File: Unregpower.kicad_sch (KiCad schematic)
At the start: 22 parts, among them J10 Conn_01x03_Female, J11 Conn_01x08_Female, J12 Conn_01x03_Female, J13 Conn_01x08_Female, J14 Conn_01x03_Female

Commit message: last TH mounting board
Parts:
- C21, C22, C26: renamed from C?; footprint (none) -> Capacitor_SMD:C_0603_1608Metric
- C23: renamed from C1; footprint Capacitor_THT:CP_Radial_D8.0mm_P3.50mm -> Capacitor_SMD:C_Elec_8x6.2; Availability (none) -> Back order
- C24: renamed from C2; footprint Capacitor_THT:CP_Radial_D8.0mm_P3.50mm -> Capacitor_SMD:C_Elec_8x6.2; Availability (none) -> Back order
- C25: renamed from C?; value C_Small -> 0.1uF; footprint (none) -> Capacitor_SMD:C_0603_1608Metric
- D1, D2, D3, D4, D5, D6: value D -> S1K-13-F; footprint Diode_THT:D_T-1_P10.16mm_Horizontal -> Diode_SMD:D_SMA
- TR1: Availability (none) -> Arrived
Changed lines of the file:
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@@
       (effects (font (size 1.27 1.27)) (justify left))
     )
-    (property "Value" "D" (id 1) (at 114.808 93.853 90)
-      (effects (font (size 1.27 1.27)) (justify left))
-    )
-    (property "Footprint" "Diode_THT:D_T-1_P10.16mm_Horizontal" (id 2) (at 112.776 94.996 0)
+    (property "Value" "S1K-13-F" (id 1) (at 114.808 93.853 90)
+      (effects (font (size 1.27 1.27)) (justify left))
+    )
+    (property "Footprint" "Diode_SMD:D_SMA" (id 2) (at 112.776 94.996 0)
       (effects (font (size 1.27 1.27)) hide)
     )
@@
       (effects (font (size 1.27 1.27)) (justify right))
     )
-    (property "Value" "D" (id 1) (at 126.238 93.853 90)
-      (effects (font (size 1.27 1.27)) (justify right))
-    )
-    (property "Footprint" "Diode_THT:D_T-1_P10.16mm_Horizontal" (id 2) (at 124.206 94.996 0)
+    (property "Value" "S1K-13-F" (id 1) (at 126.238 93.853 90)
+      (effects (font (size 1.27 1.27)) (justify right))
+    )
+    (property "Footprint" "Diode_SMD:D_SMA" (id 2) (at 124.206 94.996 0)
       (effects (font (size 1.27 1.27)) hide)
     )
@@
   (symbol (lib_id "power:PWR_FLAG") (at 102.616 107.696 90) (unit 1)
     (in_bom yes) (on_board yes)
-    (property "Reference" "#FLG05" (id 0) (at 100.711 107.696 0)
+    (property "Reference" "#FLG04" (id 0) (at 100.711 107.696 0)
       (effects (font (size 1.27 1.27)) hide)
     )
@@
       (effects (font (size 1.27 1.27)) (justify right))
     )
-    (property "Value" "D" (id 1) (at 110.744 86.233 90)
-      (effects (font (size 1.27 1.27)) (justify right))
-    )
-    (property "Footprint" "Diode_THT:D_T-1_P10.16mm_Horizontal" (id 2) (at 112.776 87.376 0)
+    (property "Value" "S1K-13-F" (id 1) (at 110.744 86.233 90)
+      (effects (font (size 1.27 1.27)) (justify right))
+    )
+    (property "Footprint" "Diode_SMD:D_SMA" (id 2) (at 112.776 87.376 0)
       (effects (font (size 1.27 1.27)) hide)
     )
@@
   (symbol (lib_id "minipowersupply-rescue:CP-Device") (at 121.666 114.046 0) (unit 1)
     (in_bom yes) (on_board yes)
-    (property "Reference" "C2" (id 0) (at 124.6632 112.8776 0)
+    (property "Reference" "C24" (id 0) (at 124.6632 112.8776 0)
       (effects (font (size 1.27 1.27)) (justify left))
     )
@@
       (effects (font (size 1.27 1.27)) (justify left))
     )
-    (property "Footprint" "Capacitor_THT:CP_Radial_D8.0mm_P3.50mm" (id 2) (at 122.6312 117.856 0)
+    (property "Footprint" "Capacitor_SMD:C_Elec_8x6.2" (id 2) (at 122.6312 117.856 0)
       (effects (font (size 1.27 1.27)) hide)
     )
@@
       (effects (font (size 1.27 1.27)) hide)
     )
+    (property "Availability" "Back order" (id 4) (at 121.666 114.046 0)
+      (effects (font (size 1.27 1.27)) hide)
+    )
     (pin "1")
     (pin "2")
@@
       (effects (font (size 1.27 1.27)) (justify left))
     )
-    (property "Value" "D" (id 1) (at 126.238 86.233 90)
-      (effects (font (size 1.27 1.27)) (justify left))
-    )
-    (property "Footprint" "Diode_THT:D_T-1_P10.16mm_Horizontal" (id 2) (at 124.206 87.376 0)
+    (property "Value" "S1K-13-F" (id 1) (at 126.238 86.233 90)
+      (effects (font (size 1.27 1.27)) (justify left))
+    )
+    (property "Footprint" "Diode_SMD:D_SMA" (id 2) (at 124.206 87.376 0)
       (effects (font (size 1.27 1.27)) hide)
     )
@@
   (symbol (lib_id "Device:C_Small") (at 187.452 83.566 0) (unit 1)
     (in_bom yes) (on_board yes) (fields_autoplaced)
-    (property "Reference" "C?" (id 0) (at 189.7761 82.7376 0)
+    (property "Reference" "C21" (id 0) (at 189.7761 82.7376 0)
       (effects (font (size 1.27 1.27)) (justify left))
     )
@@
       (effects (font (size 1.27 1.27)) (justify left))
     )
-    (property "Footprint" "" (id 2) (at 187.452 83.566 0)
+    (property "Footprint" "Capacitor_SMD:C_0603_1608Metric" (id 2) (at 187.452 83.566 0)
       (effects (font (size 1.27 1.27)) hide)
     )
@@
     (in_bom yes) (on_board yes)
     (property "Reference" "D1" (id 0) (at 135.636 78.0542 0))
-    (property "Value" "D" (id 1) (at 135.636 80.3656 0))
-    (property "Footprint" "Diode_THT:D_T-1_P10.16mm_Horizontal" (id 2) (at 135.636 83.566 0)
+    (property "Value" "S1K-13-F" (id 1) (at 135.636 80.3656 0))
+    (property "Footprint" "Diode_SMD:D_SMA" (id 2) (at 135.636 83.566 0)
       (effects (font (size 1.27 1.27)) hide)
     )
@@
   (symbol (lib_id "Device:C_Small") (at 180.594 108.966 0) (unit 1)
     (in_bom yes) (on_board yes) (fields_autoplaced)
-    (property "Reference" "C?" (id 0) (at 182.9181 108.1376 0)
+    (property "Reference" "C22" (id 0) (at 182.9181 108.1376 0)
       (effects (font (size 1.27 1.27)) (justify left))
     )
@@
       (effects (font (size 1.27 1.27)) (justify left))
     )
-    (property "Footprint" "" (id 2) (at 180.594 108.966 0)
+    (property "Footprint" "Capacitor_SMD:C_0603_1608Metric" (id 2) (at 180.594 108.966 0)
       (effects (font (size 1.27 1.27)) hide)
     )
@@
     (in_bom yes) (on_board yes)
     (property "Reference" "D6" (id 0) (at 135.636 101.346 0))
-    (property "Value" "D" (id 1) (at 135.636 96.266 0))
-    (property "Footprint" "Diode_THT:D_T-1_P10.16mm_Horizontal" (id 2) (at 135.636 98.806 0)
+    (property "Value" "S1K-13-F" (id 1) (at 135.636 96.266 0))
+    (property "Footprint" "Diode_SMD:D_SMA" (id 2) (at 135.636 98.806 0)
       (effects (font (size 1.27 1.27)) hide)
     )
@@
   (symbol (lib_id "minipowersupply-rescue:CP-Device") (at 102.616 114.046 180) (unit 1)
     (in_bom yes) (on_board yes)
-    (property "Reference" "C1" (id 0) (at 105.6132 112.8776 0)
+    (property "Reference" "C23" (id 0) (at 105.6132 112.8776 0)
       (effects (font (size 1.27 1.27)) (justify right))
     )
@@
       (effects (font (size 1.27 1.27)) (justify right))
     )
-    (property "Footprint" "Capacitor_THT:CP_Radial_D8.0mm_P3.50mm" (id 2) (at 101.6508 110.236 0)
+    (property "Footprint" "Capacitor_SMD:C_Elec_8x6.2" (id 2) (at 101.6508 110.236 0)
       (effects (font (size 1.27 1.27)) hide)
     )
     (property "Datasheet" "~" (id 3) (at 102.616 114.046 0)
+      (effects (font (size 1.27 1.27)) hide)
+    )
+    (property "Availability" "Back order" (id 4) (at 102.616 114.046 0)
       (effects (font (size 1.27 1.27)) hide)
     )
@@
   (symbol (lib_id "Device:C_Small") (at 185.928 129.286 0) (unit 1)
     (in_bom yes) (on_board yes) (fields_autoplaced)
-    (property "Reference" "C?" (id 0) (at 188.2521 128.4576 0)
+    (property "Reference" "C26" (id 0) (at 188.2521 128.4576 0)
       (effects (font (size 1.27 1.27)) (justify left))
     )
@@
       (effects (font (size 1.27 1.27)) (justify left))
     )
-    (property "Footprint" "" (id 2) (at 185.928 129.286 0)
+    (property "Footprint" "Capacitor_SMD:C_0603_1608Metric" (id 2) (at 185.928 129.286 0)
       (effects (font (size 1.27 1.27)) hide)
     )
@@
   (symbol (lib_id "power:PWR_FLAG") (at 96.266 83.566 0) (unit 1)
     (in_bom yes) (on_board yes)
-    (property "Reference" "#FLG02" (id 0) (at 96.266 81.661 0)
+    (property "Reference" "#FLG01" (id 0) (at 96.266 81.661 0)
       (effects (font (size 1.27 1.27)) hide)
     )
@@
   (symbol (lib_id "Device:C_Small") (at 185.928 119.126 0) (unit 1)
     (in_bom yes) (on_board yes) (fields_autoplaced)
-    (property "Reference" "C?" (id 0) (at 188.2521 118.2976 0)
-      (effects (font (size 1.27 1.27)) (justify left))
-    )
-    (property "Value" "C_Small" (id 1) (at 188.2521 120.8345 0)
-      (effects (font (size 1.27 1.27)) (justify left))
-    )
-    (property "Footprint" "" (id 2) (at 185.928 119.126 0)
+    (property "Reference" "C25" (id 0) (at 188.2521 118.2976 0)
+      (effects (font (size 1.27 1.27)) (justify left))
+    )
+    (property "Value" "0.1uF" (id 1) (at 188.2521 120.8345 0)
+      (effects (font (size 1.27 1.27)) (justify left))
+    )
+    (property "Footprint" "Capacitor_SMD:C_0603_1608Metric" (id 2) (at 185.928 119.126 0)
       (effects (font (size 1.27 1.27)) hide)
     )
@@
   (symbol (lib_id "power:PWR_FLAG") (at 96.266 98.806 0) (unit 1)
     (in_bom yes) (on_board yes)
-    (property "Reference" "#FLG04" (id 0) (at 96.266 96.901 0)
+    (property "Reference" "#FLG03" (id 0) (at 96.266 96.901 0)
       (effects (font (size 1.27 1.27)) hide)
     )
@@
   (symbol (lib_id "power:PWR_FLAG") (at 121.666 107.696 90) (unit 1)
     (in_bom yes) (on_board yes)
-    (property "Reference" "#FLG06" (id 0) (at 119.761 107.696 0)
+    (property "Reference" "#FLG05" (id 0) (at 119.761 107.696 0)
       (effects (font (size 1.27 1.27)) hide)
     )
@@
     )
     (property "Datasheet" "" (id 3) (at 88.646 91.186 0)
+      (effects (font (size 1.27 1.27)) hide)
+    )
+    (property "Availability" "Arrived" (id 4) (at 88.646 91.186 0)
       (effects (font (size 1.27 1.27)) hide)
     )
@@
   (symbol (lib_id "power:PWR_FLAG") (at 96.266 91.186 0) (unit 1)
     (in_bom yes) (on_board yes)
-    (property "Reference" "#FLG03" (id 0) (at 96.266 89.281 0)
-      (effects (font (size 1.27 1.27)) hide)
-    )
+    (property "Reference" "#FLG02" (id 0) (at 96.266 89.281 0)
+      (effects (font (size 1.27 1.27)) hide)
+    )

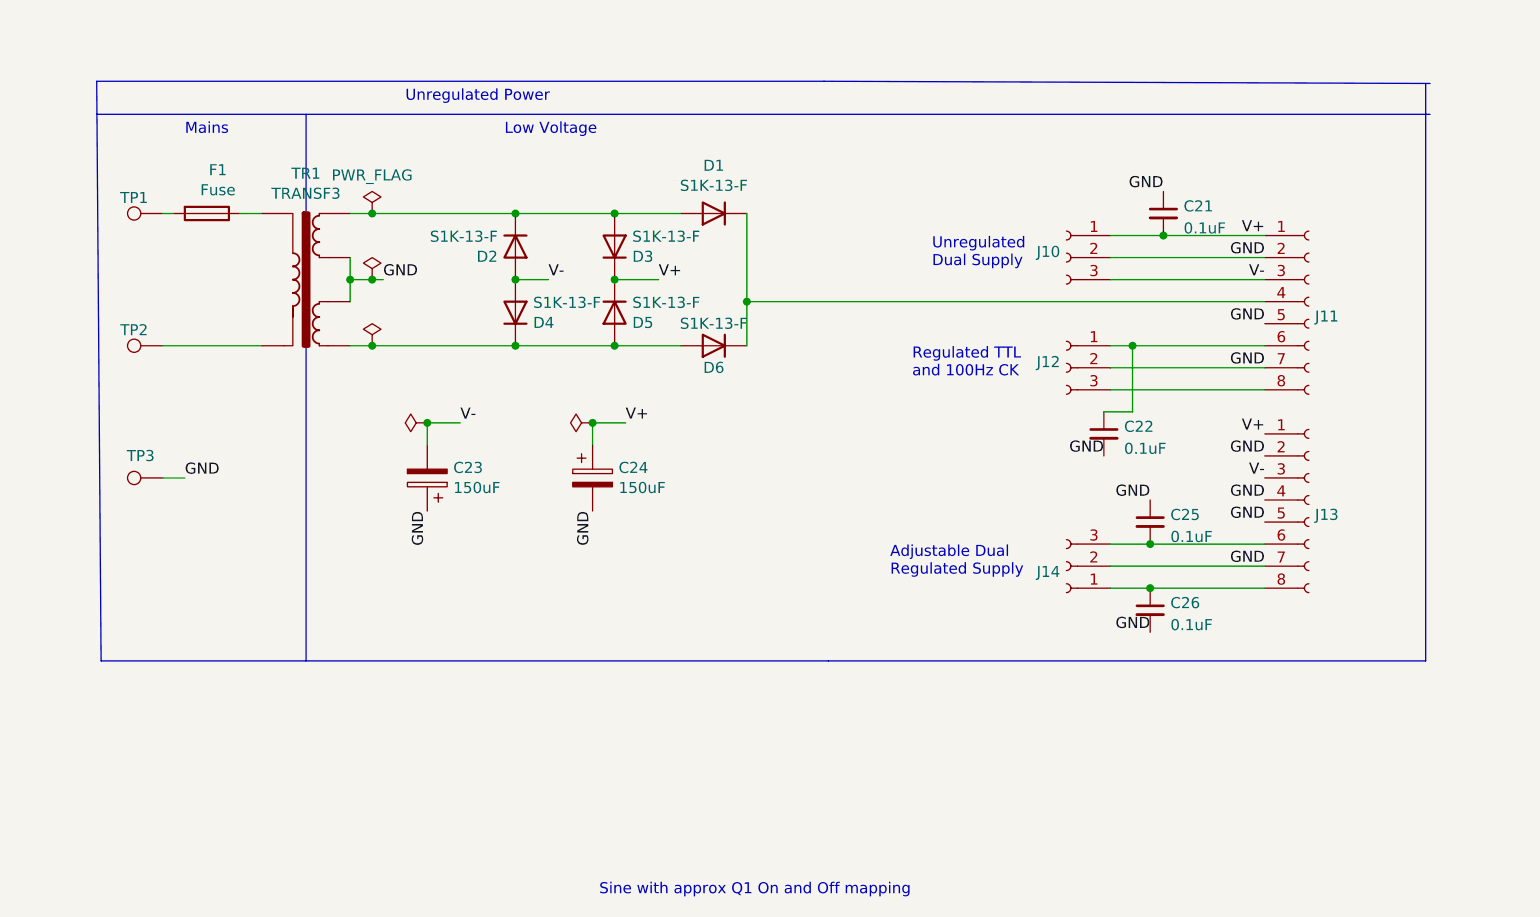
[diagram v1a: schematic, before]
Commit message: all SMD components going into boards
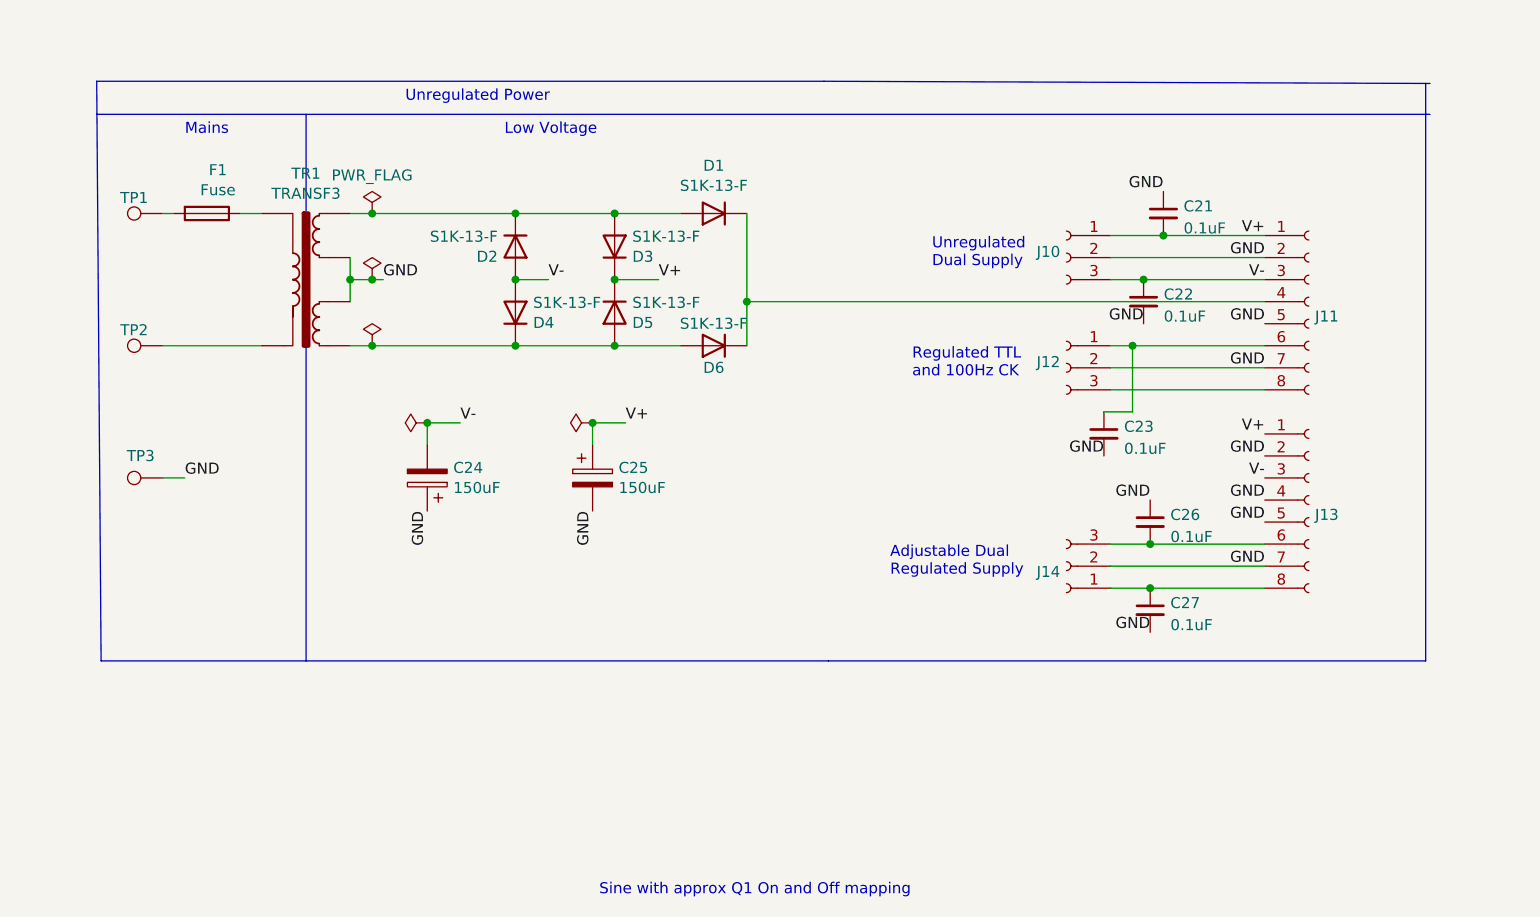
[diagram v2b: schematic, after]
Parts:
- added C22: 0.1uF, Capacitor_SMD:C_0603_1608Metric, symbol Device:C_Small
- renumbered C22 to C23, C23 to C24, C24 to C25, C25 to C26, C26 to C27
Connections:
- net GND: now also C22.2
- net V-: now also C22.1
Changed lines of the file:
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@@
   (junction (at 96.266 98.806) (diameter 0) (color 0 0 0 0)
   )
+  (junction (at 185.166 91.186) (diameter 0) (color 0 0 0 0)
+  )
   (junction (at 124.206 83.566) (diameter 0) (color 0 0 0 0)
   )
@@
     (stroke (width 0) (type default) (color 0 0 0 0))
   )
-  (wire (pts (xy 181.356 91.186) (xy 199.136 91.186))
+  (wire (pts (xy 181.356 91.186) (xy 185.166 91.186))
     (stroke (width 0) (type default) (color 0 0 0 0))
   )
@@
   )
   (wire (pts (xy 112.776 83.566) (xy 124.206 83.566))
+    (stroke (width 0) (type default) (color 0 0 0 0))
+  )
+  (wire (pts (xy 185.166 91.186) (xy 199.136 91.186))
     (stroke (width 0) (type default) (color 0 0 0 0))
   )
@@
     (effects (font (size 1.27 1.27)) (justify right bottom))
   )
+  (label "GND" (at 185.166 96.266 180)
+    (effects (font (size 1.27 1.27)) (justify right bottom))
+  )
   (label "GND" (at 185.928 131.826 180)
     (effects (font (size 1.27 1.27)) (justify right bottom))
@@
     )
     (property "Datasheet" "~" (id 3) (at 112.776 94.996 0)
+      (effects (font (size 1.27 1.27)) hide)
+    )
+    (pin "1")
+    (pin "2")
+  )
+  (symbol (lib_id "Device:C_Small") (at 185.166 93.726 0) (unit 1)
+    (in_bom yes) (on_board yes) (fields_autoplaced)
+    (property "Reference" "C22" (id 0) (at 187.4901 92.8976 0)
+      (effects (font (size 1.27 1.27)) (justify left))
+    )
+    (property "Value" "0.1uF" (id 1) (at 187.4901 95.4345 0)
+      (effects (font (size 1.27 1.27)) (justify left))
+    )
+    (property "Footprint" "Capacitor_SMD:C_0603_1608Metric" (id 2) (at 185.166 93.726 0)
+      (effects (font (size 1.27 1.27)) hide)
+    )
+    (property "Datasheet" "~" (id 3) (at 185.166 93.726 0)
       (effects (font (size 1.27 1.27)) hide)
     )
@@
   (symbol (lib_id "minipowersupply-rescue:CP-Device") (at 121.666 114.046 0) (unit 1)
     (in_bom yes) (on_board yes)
-    (property "Reference" "C24" (id 0) (at 124.6632 112.8776 0)
+    (property "Reference" "C25" (id 0) (at 124.6632 112.8776 0)
       (effects (font (size 1.27 1.27)) (justify left))
     )
@@
   (symbol (lib_id "Device:C_Small") (at 180.594 108.966 0) (unit 1)
     (in_bom yes) (on_board yes) (fields_autoplaced)
-    (property "Reference" "C22" (id 0) (at 182.9181 108.1376 0)
+    (property "Reference" "C23" (id 0) (at 182.9181 108.1376 0)
       (effects (font (size 1.27 1.27)) (justify left))
     )
@@
   (symbol (lib_id "minipowersupply-rescue:CP-Device") (at 102.616 114.046 180) (unit 1)
     (in_bom yes) (on_board yes)
-    (property "Reference" "C23" (id 0) (at 105.6132 112.8776 0)
+    (property "Reference" "C24" (id 0) (at 105.6132 112.8776 0)
       (effects (font (size 1.27 1.27)) (justify right))
     )
@@
   (symbol (lib_id "Device:C_Small") (at 185.928 129.286 0) (unit 1)
     (in_bom yes) (on_board yes) (fields_autoplaced)
-    (property "Reference" "C26" (id 0) (at 188.2521 128.4576 0)
+    (property "Reference" "C27" (id 0) (at 188.2521 128.4576 0)
       (effects (font (size 1.27 1.27)) (justify left))
     )
@@
   (symbol (lib_id "Device:C_Small") (at 185.928 119.126 0) (unit 1)
     (in_bom yes) (on_board yes) (fields_autoplaced)
-    (property "Reference" "C25" (id 0) (at 188.2521 118.2976 0)
-      (effects (font (size 1.27 1.27)) (justify left))
-    )
+    (property "Reference" "C26" (id 0) (at 188.2521 118.2976 0)
+      (effects (font (size 1.27 1.27)) (justify left))
+    )

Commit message: new board with SMD
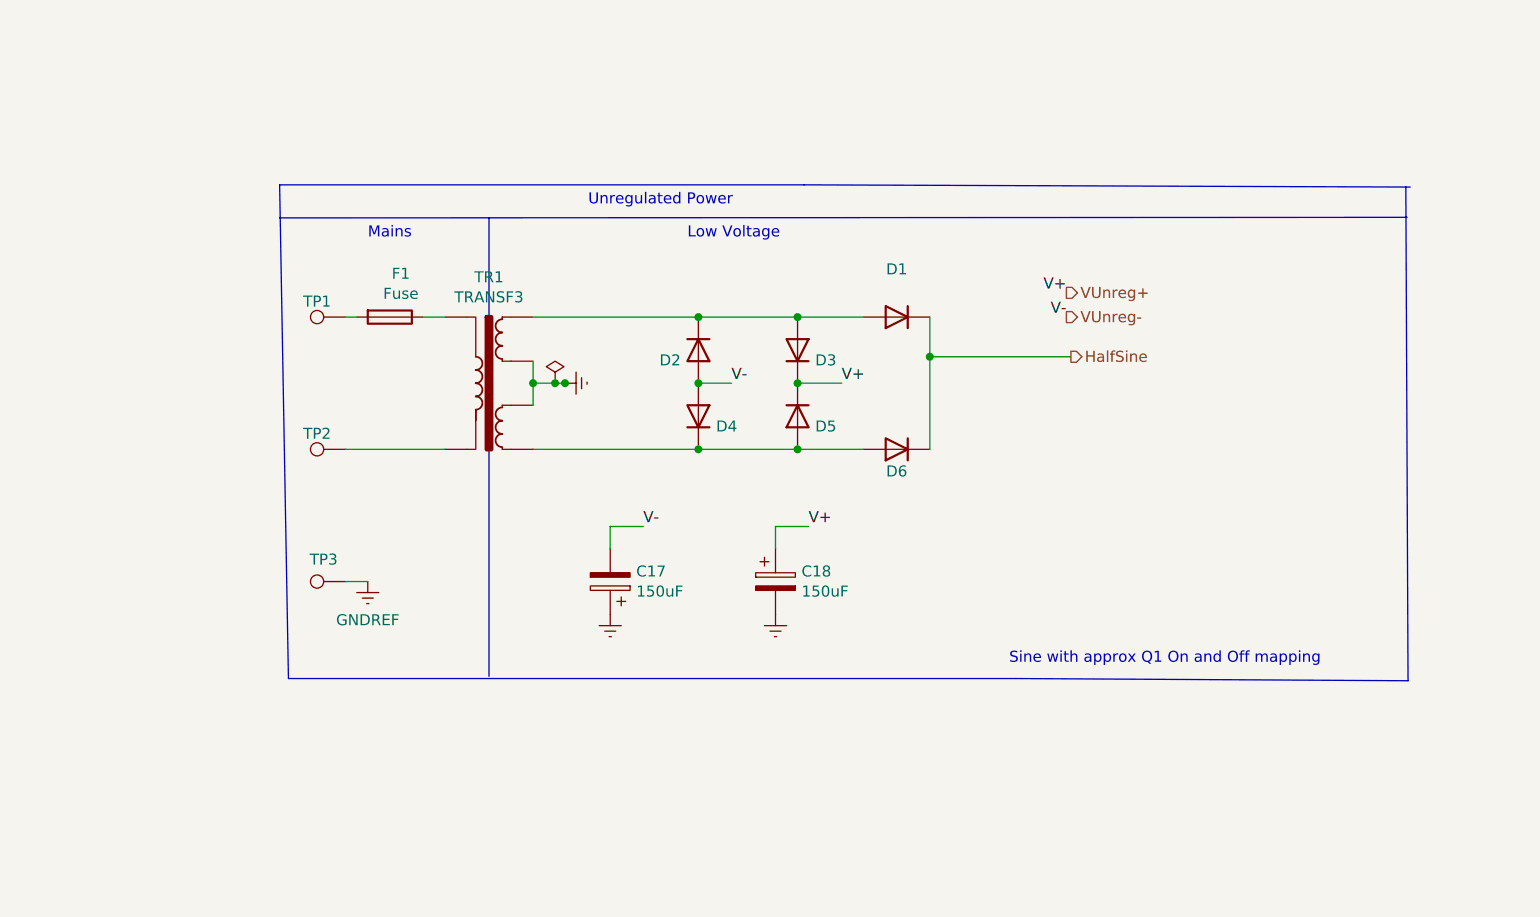
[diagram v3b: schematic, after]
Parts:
- removed C21, C22, C23, C26, C27: 0.1uF, Capacitor_SMD:C_0603_1608Metric, symbol Device:C_Small
- removed J10, J12, J14: Conn_01x03_Female, Connector_PinHeader_2.54mm:PinHeader_1x03_P2.54mm_Vertical, symbol Connector:Conn_01x03_Female
- removed J11, J13: Conn_01x08_Female, Connector_PinHeader_2.54mm:PinHeader_1x08_P2.54mm_Vertical, symbol Connector:Conn_01x08_Female
- renumbered C24 to C17, C25 to C18
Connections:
- net HalfSine: now reaches D1.1 (K), D6.1 (K)
- net GND renamed GNDREF
- net V+ renamed VUnreg+
- net V- renamed VUnreg-
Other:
- note removed: "Adjustable Dual Regulated Supply"
- note removed: "Regulated TTL and 100Hz CK"
- note removed: "Unregulated Dual Supply"
- moved on the sheet: C17, C18, D1, D2, D3, D4, D5, D6, F1, TP1, TP2, TP3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
